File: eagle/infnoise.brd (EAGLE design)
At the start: 34.3 x 12 mm, 25 parts, among them SW1 NS5B1G385DFT2G, SW2 NS5B1G385DFT2G, U1 FT240XQ, X1 USBPCB

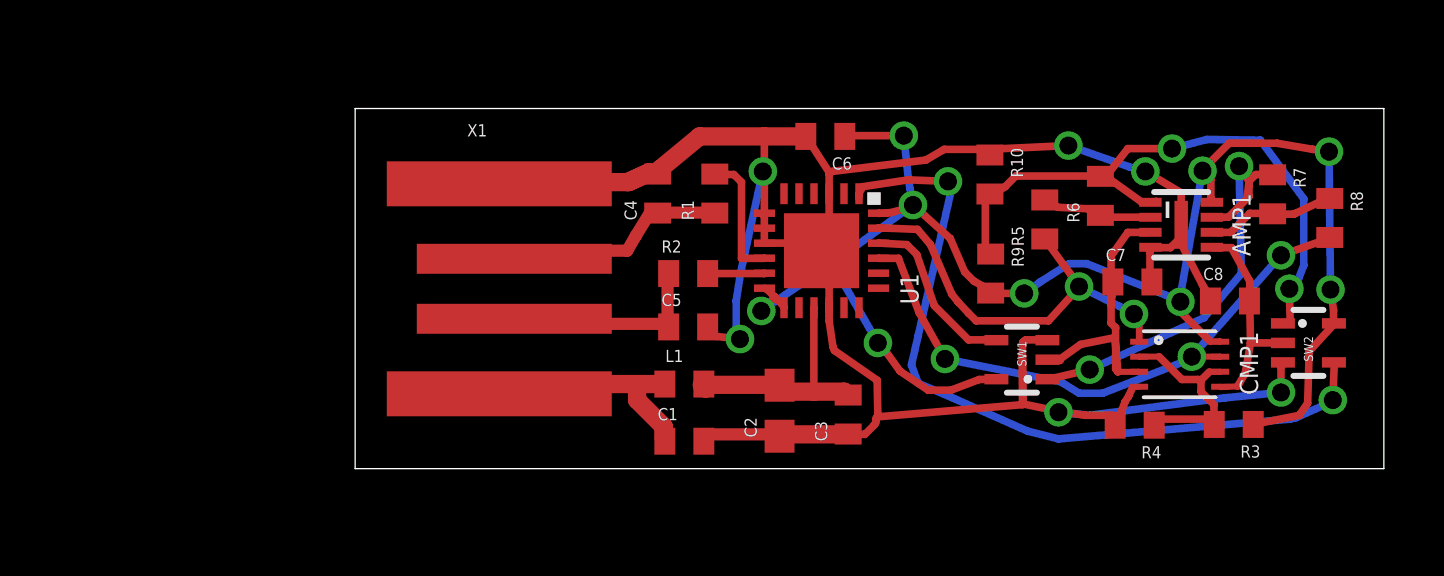
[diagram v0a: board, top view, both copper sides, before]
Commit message: Added bitmap of board to README
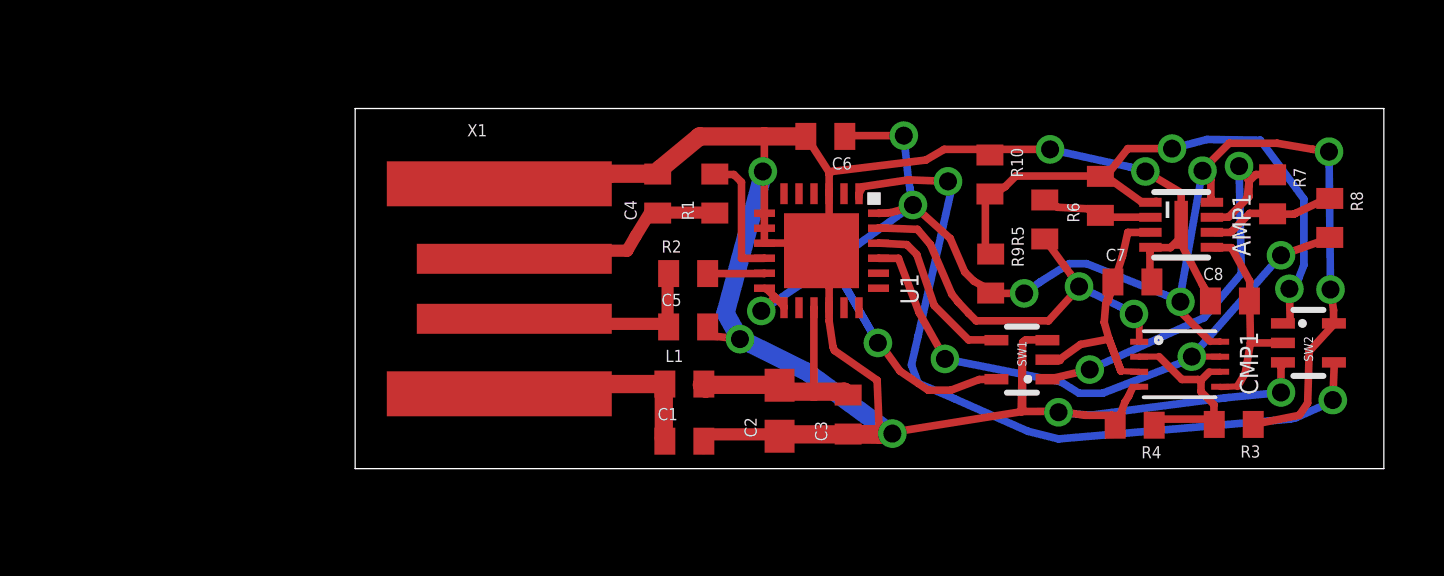
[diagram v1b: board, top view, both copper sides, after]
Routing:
- net GND: track 83.1 -> 98.1 mm, vias 6 -> 7
- net VCC33: track 55.4 -> 58.4 mm

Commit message: minor cleanup
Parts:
- removed AMP1: TSV912IQ2T, infnoise:DFN6-2X3
- added AMP: TSV912IQ2T, infnoise:DFN6-2X3
- moved R9 0.29 mm to (21.1, 6.78), turned to 90 degrees
- moved R5 0.26 mm to (23.0, 8.05)
- moved R10 0.18 mm to (21.1, 9.98)
- moved C7 0.08 mm to (25.9, 6.30)
- renumbered CMP1 to CMP
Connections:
- net A: now also AMP.3; no longer AMP1.3
- net AMP1OUT: now also AMP.1, R9.2; no longer AMP1.1, R9.1
- net AMP2OUT: now also AMP.7; no longer AMP1.7
- net B: now also AMP.5; no longer AMP1.5
- net FB1: now also AMP.2; no longer AMP1.2
- net FB2: now also AMP.6; no longer AMP1.6
- net GND: now also AMP.4, AMP.EXP; no longer AMP1.4, AMP1.EXP
- net VCC33: now also AMP.8, R9.1; no longer AMP1.8, R9.2
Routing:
- net VCC33: track 58.4 -> 55.4 mm
- net COMP1: track 14.2 -> 13.4 mm
- net AMP1OUT: track 21.2 -> 21.9 mm

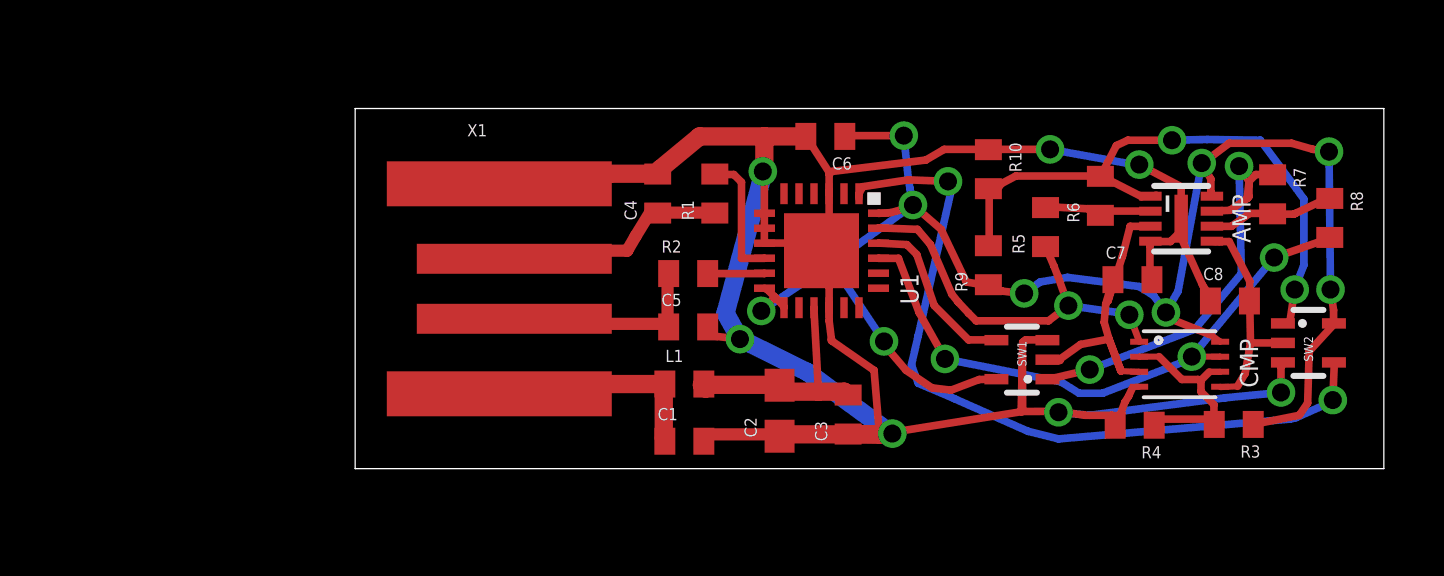
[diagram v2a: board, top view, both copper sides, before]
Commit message: Increased widths and spacing based on advice on web
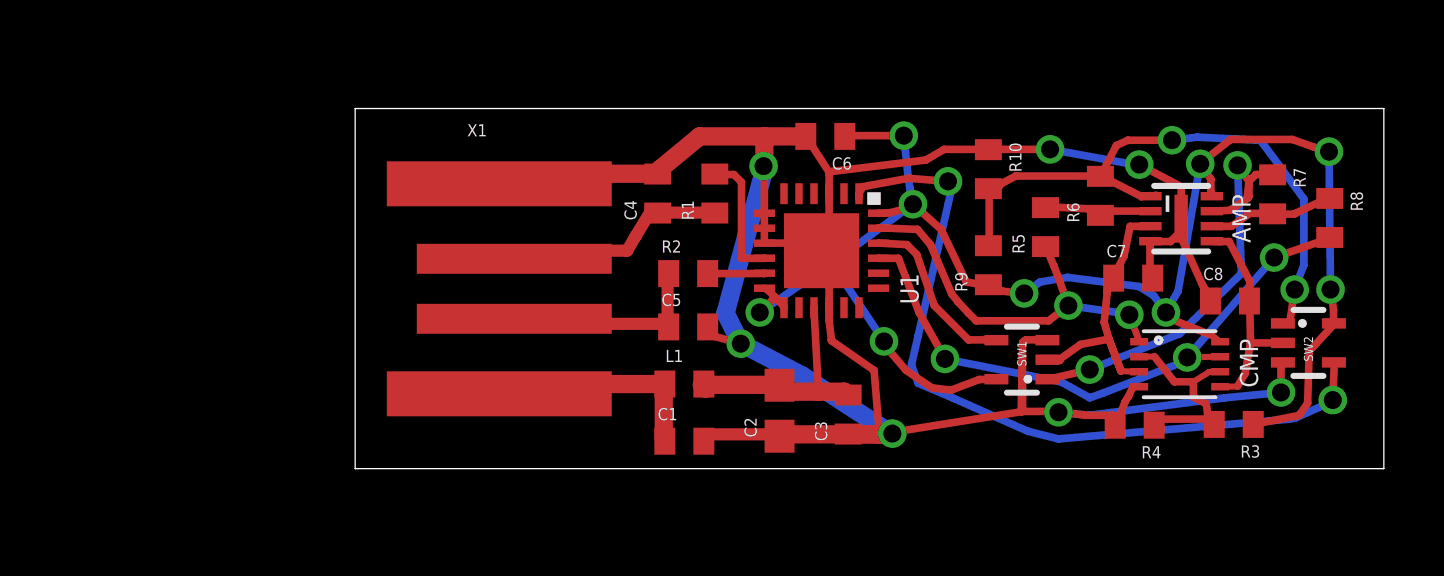
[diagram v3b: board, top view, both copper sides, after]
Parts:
- moved C7 0.06 mm to (25.9, 6.35)
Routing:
- net A: track 11.4 -> 10.6 mm
- net GND: track 98.5 -> 99.1 mm

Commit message: Changed to real USB connector
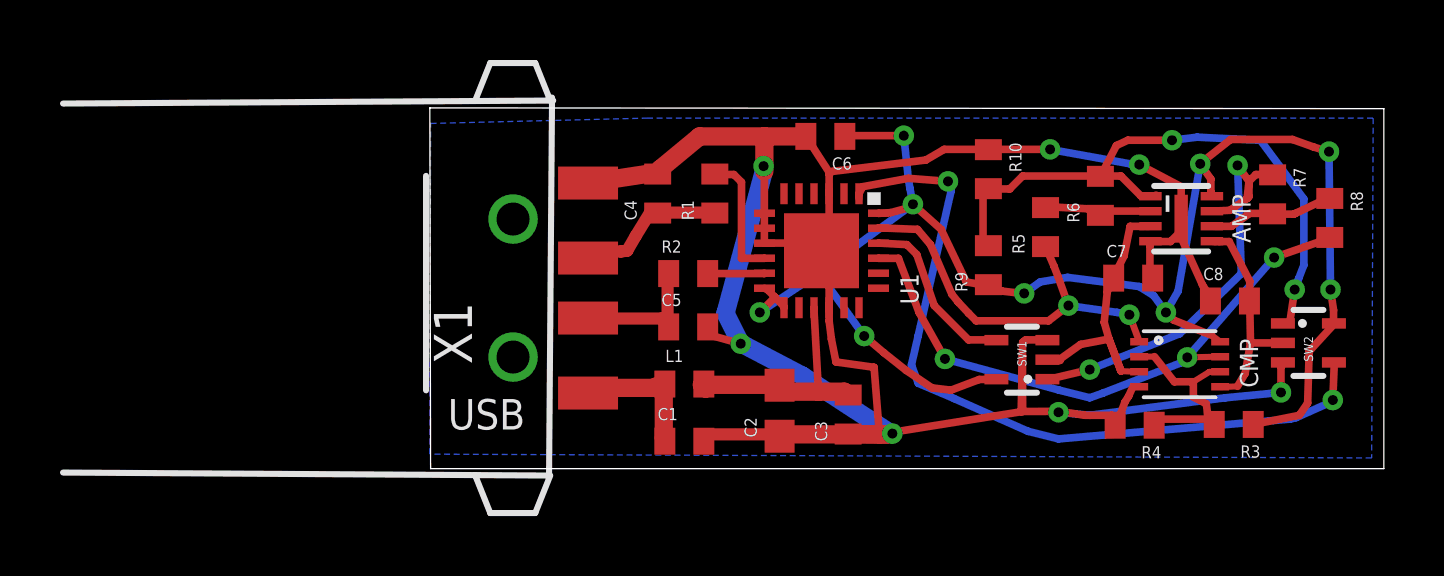
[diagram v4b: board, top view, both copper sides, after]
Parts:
- X1: value USBPCB -> USBCON; device infnoise:USB-A-PCB -> infnoise:USB-A-CON
- moved X1 3.76 mm to (8.76, 6.02), turned to 270 degrees
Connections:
- net GND: now also X1.4, X1.H1, X1.H2; no longer X1.GND
- net USB_M: now also X1.3; no longer X1.USB_P
- net USB_P: now also X1.2; no longer X1.USB_M
- net VCC5: now also X1.1; no longer X1.5V
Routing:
- net GND: track 99.1 -> 96.7 mm
- net VCC5: track 7.65 -> 5.24 mm
- net USB_P: track 7.09 -> 5.18 mm
- net USB_M: track 7.54 -> 6.58 mm
- net AMP1OUT: track 21.9 -> 21.2 mm
- added copper zone on layer 16, net GND
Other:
- board size 34.3 x 12 mm -> 31.8 x 12 mm
